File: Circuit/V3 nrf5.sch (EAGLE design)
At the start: 58 parts, among them J4 USB Micro, J7 CORTEX_DEBUG_SMD, Q1 FDV301N, Q2 BSS84, Q3 FDV301N, U2 MCP73831, U3 BC840M, U4 MIC5205, U8 TPS61236P, Y1 32.768kHz

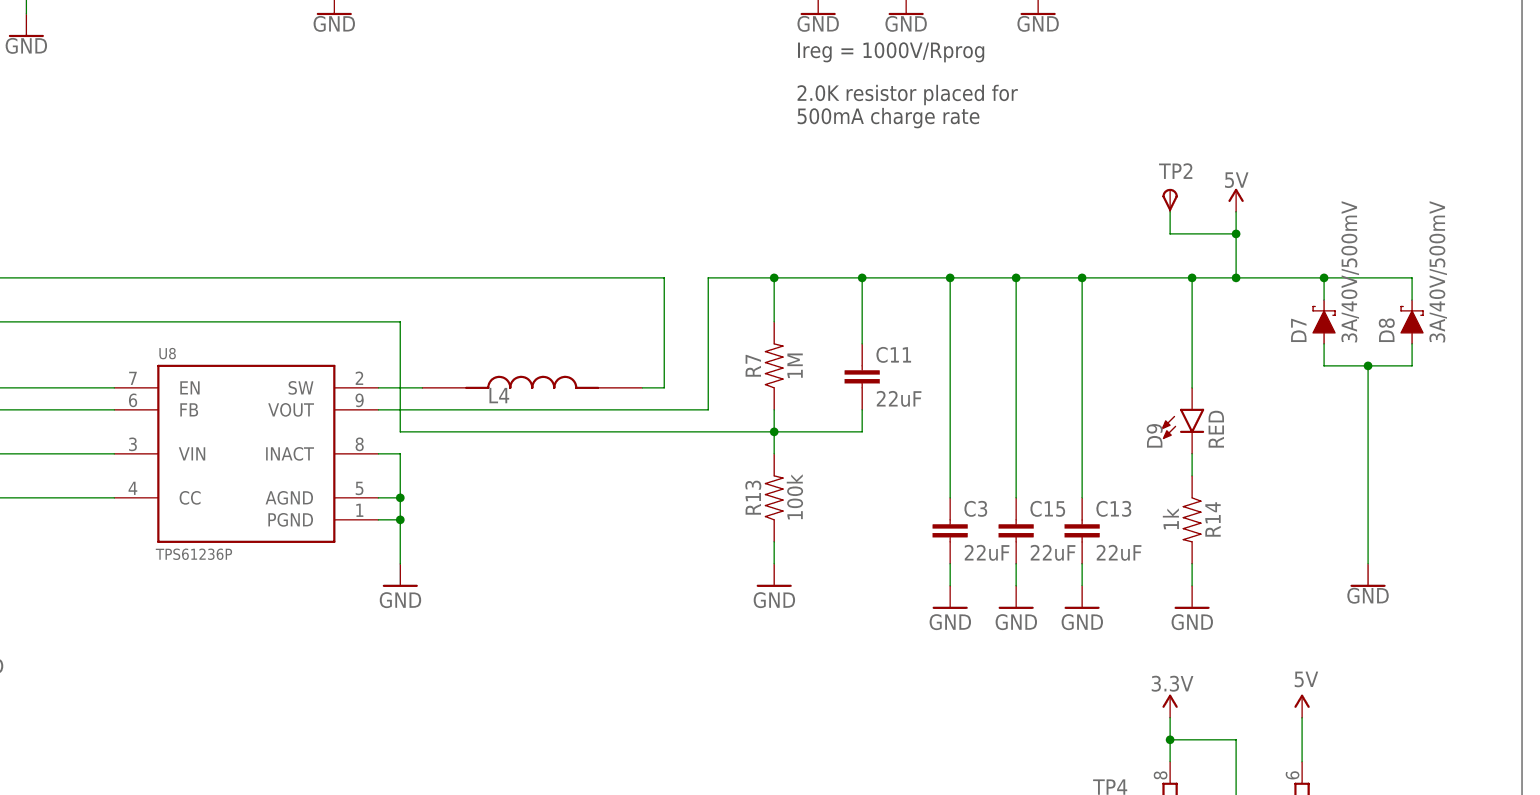
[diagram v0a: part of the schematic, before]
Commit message: Updating with in stock digikey components. Subbing adjustable boost converter for fixed.
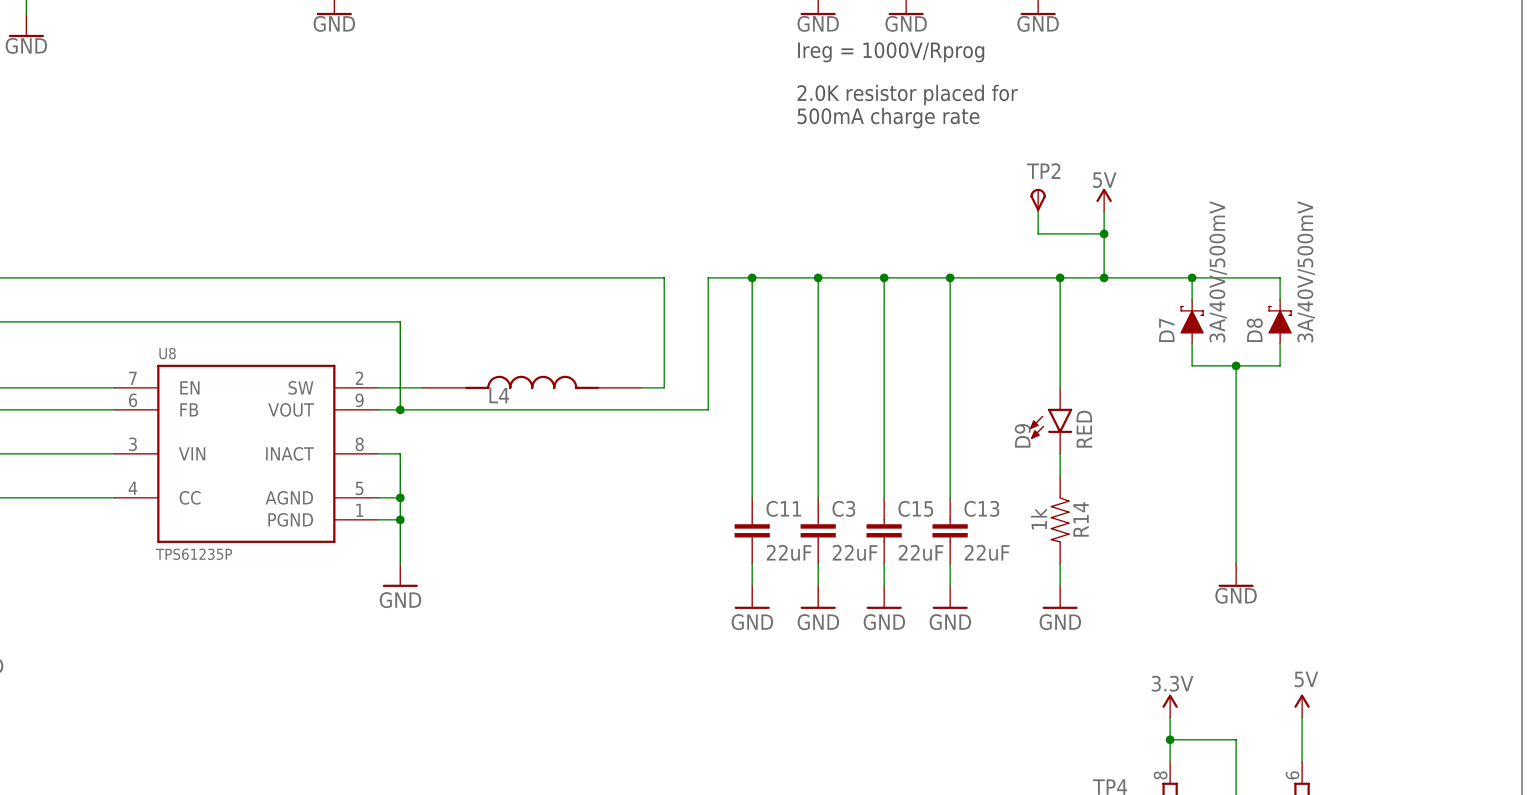
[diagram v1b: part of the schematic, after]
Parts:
- removed R13: 100k, SparkFun-Resistors:100KOHM-0603-1/10W-1%
- removed R7: 1M, SparkFun-Resistors:750KOHM-0603-1/10W-1%
- D10: DIGIKEY MBR120VLSFT1G -> SM5817PL-TPMSCT-ND‎
- D7: DIGIKEY B340A-E3/61TGICT-ND -> B340A-FDITR-ND
- RPROG: DIGIKEY P2.00KHCT-ND -> ‎311-2.00KHRCT-ND‎
- U8: value TPS61236P -> TPS61235P; DIGIKEY 296-44629-1-ND -> 296-47376-2-ND
- Y1: DIGIKEY 1923-1342-1-ND -> 1908-1314-2-ND
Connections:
- removed net N$9: C11.2, R13.2, R7.1, U8.FB
- net 5V: now also U8.FB; no longer R7.2
- net GND: now also C11.2; no longer R13.1
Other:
- moved on the sheet: C11, C13, C15, C3, D7, D8, D9, R14, TP2

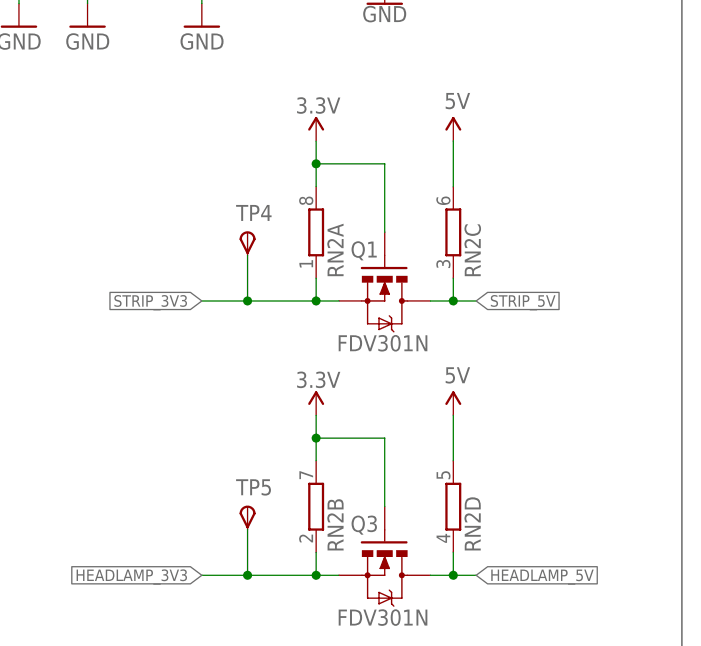
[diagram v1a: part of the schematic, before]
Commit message: Layout of component name and adding the value of the 10k.
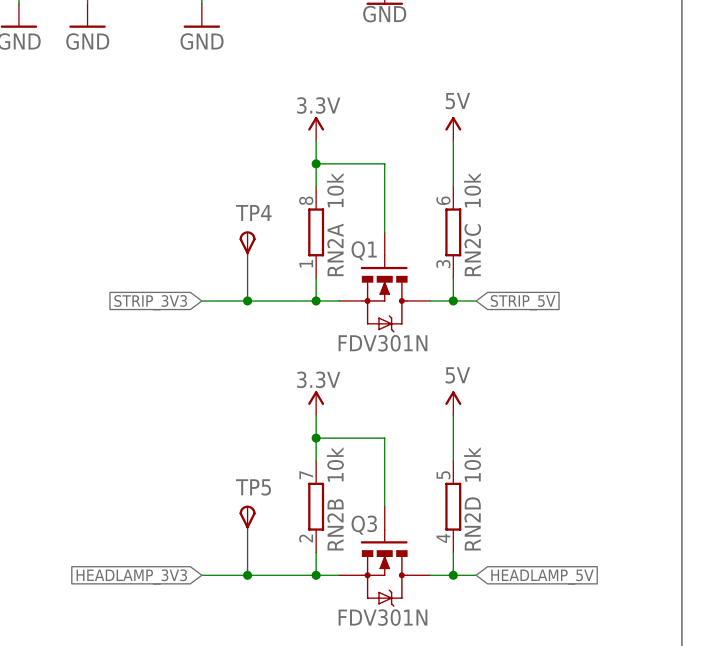
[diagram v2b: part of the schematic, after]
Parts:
- RN2: value (none) -> 10k
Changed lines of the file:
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@@
 <part name="TP5" library="testpad" library_urn="urn:adsk.eagle:library:385" deviceset="TPS" device="B1,27" package3d_urn="urn:adsk.eagle:package:27944/2"/>
 <part name="P+8" library="SparkFun" deviceset="3.3V" device="" value="3.3V"/>
-<part name="RN2" library="resistor-dil" library_urn="urn:adsk.eagle:library:342" deviceset="4R-N" device="EXBV8V" package3d_urn="urn:adsk.eagle:package:24931/1">
+<part name="RN2" library="resistor-dil" library_urn="urn:adsk.eagle:library:342" deviceset="4R-N" device="EXBV8V" package3d_urn="urn:adsk.eagle:package:24931/1" value="10k">
 <attribute name="DIGIKEY" value="YC164-JR-0710KL"/>
 </part>

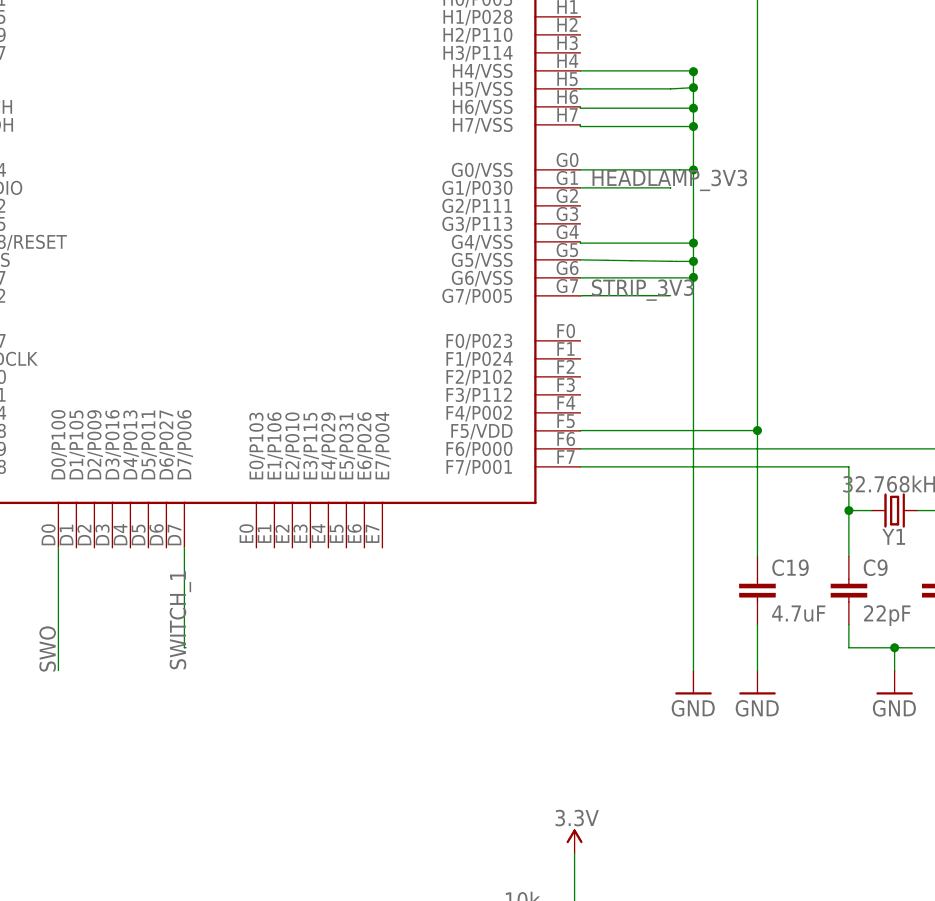
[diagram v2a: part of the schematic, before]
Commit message: Switching headlamp to P0.06 (and sending the switch to P0.30). Needs routing.
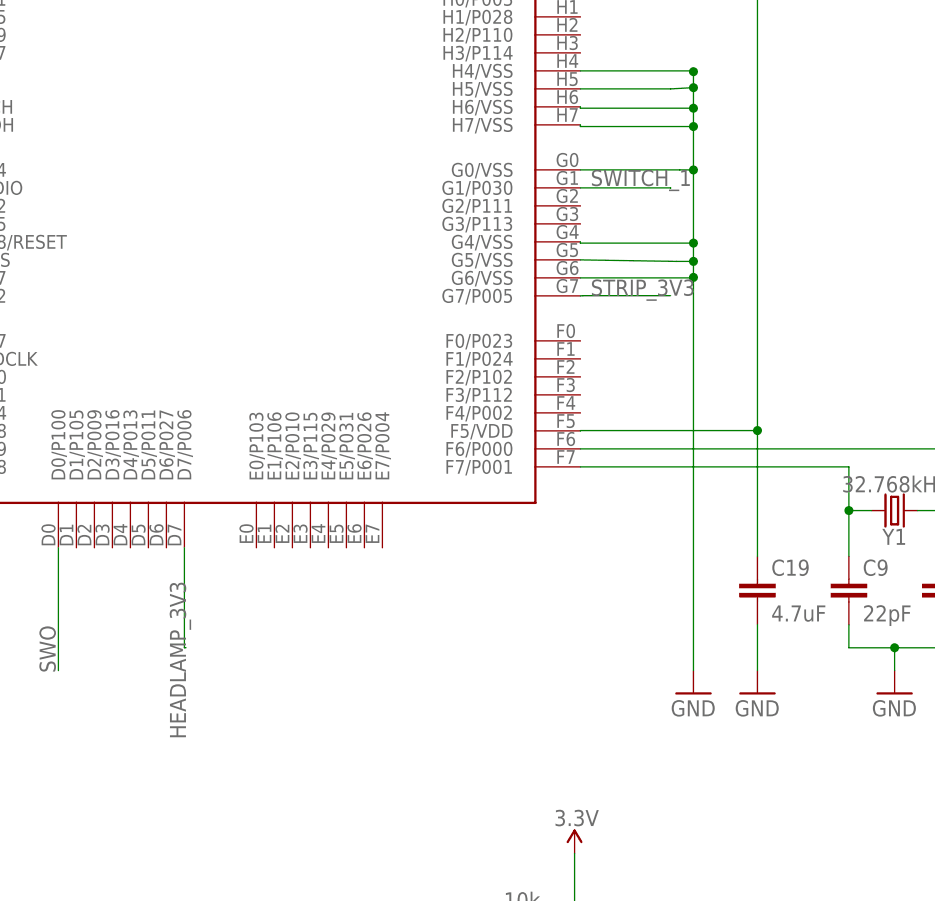
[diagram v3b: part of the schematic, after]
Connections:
- net HEADLAMP_3V3: now also U3.D7/P006; no longer U3.G1/P030
- net SWITCH_1: now also U3.G1/P030; no longer U3.D7/P006
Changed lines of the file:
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@@
 </segment>
 <segment>
-<pinref part="U3" gate="G$1" pin="D7/P006"/>
-<wire x1="81.106" y1="97.454" x2="81.106" y2="86.36" width="0.1524" layer="91"/>
-<wire x1="81.106" y1="86.36" x2="81.28" y2="86.36" width="0.1524" layer="91"/>
-<label x="81.28" y="83.82" size="1.778" layer="95" rot="R90"/>
+<pinref part="U3" gate="G$1" pin="G1/P030"/>
+<wire x1="125.106" y1="137.454" x2="135.128" y2="137.454" width="0.1524" layer="91"/>
+<wire x1="135.128" y1="137.454" x2="135.128" y2="137.414" width="0.1524" layer="91"/>
+<label x="126.238" y="137.668" size="1.778" layer="95"/>
 </segment>
 </net>
@@
 </segment>
 <segment>
-<pinref part="U3" gate="G$1" pin="G1/P030"/>
-<wire x1="125.106" y1="137.454" x2="135.128" y2="137.454" width="0.1524" layer="91"/>
-<wire x1="135.128" y1="137.454" x2="135.128" y2="137.414" width="0.1524" layer="91"/>
-<label x="126.238" y="137.668" size="1.778" layer="95"/>
-</segment>
-</net>
+<pinref part="U3" gate="G$1" pin="D7/P006"/>
+<wire x1="81.106" y1="97.454" x2="81.106" y2="86.36" width="0.1524" layer="91"/>
+<wire x1="81.106" y1="86.36" x2="81.28" y2="86.36" width="0.1524" layer="91"/>
+<label x="81.28" y="76.2" size="1.778" layer="95" rot="R90"/>
+</segment>
+</net>

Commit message: board update
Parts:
- removed Q1, Q3: FDV301N, SparkFun:MOSFET-NCHANNELSMD
- removed RN2: 10k, resistor-dil:4R-NEXBV8V
- added U1: 74AHCT2G125, cdclvc11xx_10:74AHCT2G125
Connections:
- new net N$9: J6.1, J6.2
- net 3.3V: no longer Q1.G, Q3.G, RN2A.2, RN2B.2
- net 5V: now also J6.4, U1.VCC; no longer J6.1, RN2C.2, RN2D.2
- net GND: now also U1.1!OE, U1.2!OE, U1.GND; no longer J6.3, J6.4
- net HEADLAMP_3V3: now also TP4.PP, U1.2A; no longer Q3.S, RN2B.1, TP5.PP
- net HEADLAMP_5V: now also U1.2Y; no longer Q3.D, RN2D.1
- net N$2: now also J6.3; no longer J6.2
- net STRIP_3V3: now also TP5.PP, U1.1A, U3.E7/P004; no longer Q1.S, RN2A.1, TP4.PP, U3.G7/P005
- net STRIP_5V: now also U1.1Y; no longer Q1.D, RN2C.1
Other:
- moved on the sheet: R10, TP4, TP5
